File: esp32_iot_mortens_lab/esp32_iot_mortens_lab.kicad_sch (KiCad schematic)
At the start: 5 parts, among them P1 USB_C_Plug_USB2.0, Q1 UMH3N, U1 ESP32-WROOM-32D, U2 USBLC6-2P6, U3 CP2104

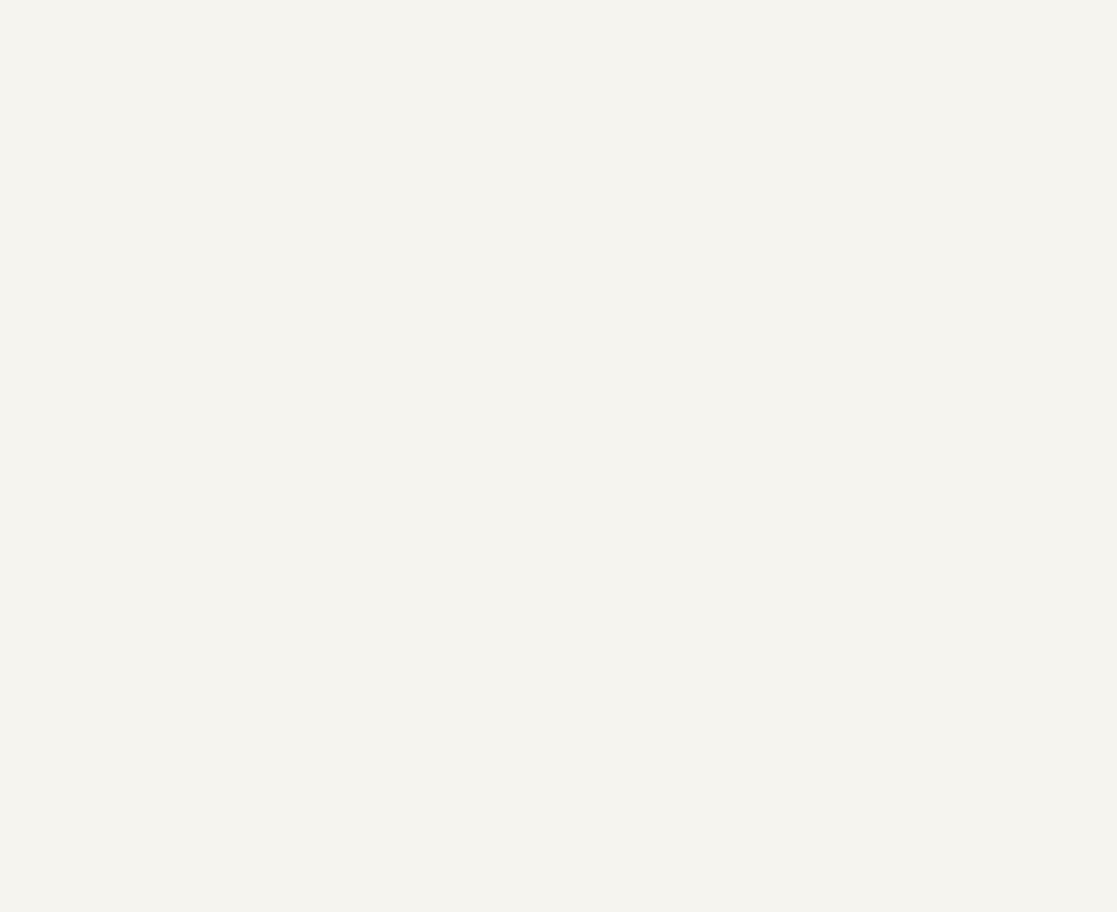
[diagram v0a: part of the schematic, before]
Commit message: upto J2 screw
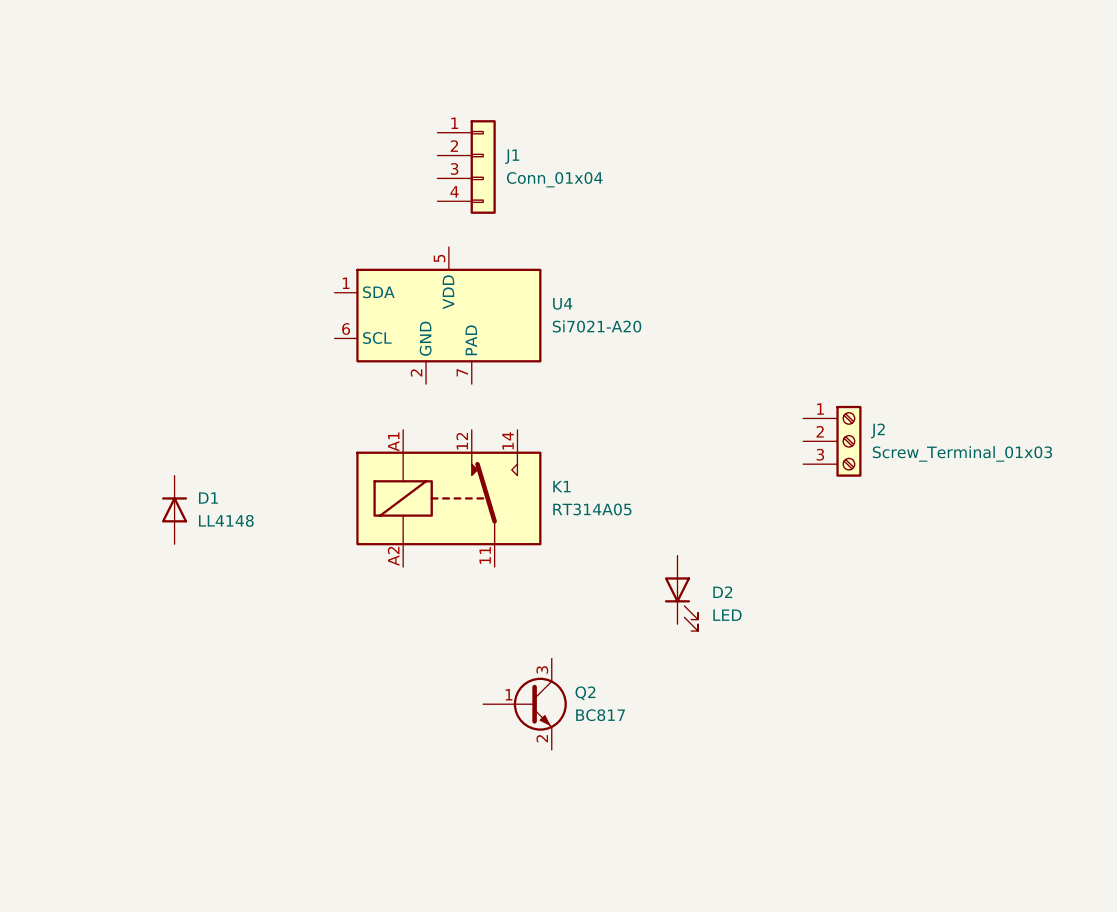
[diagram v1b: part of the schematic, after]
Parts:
- added D1: LL4148, Diode_SMD:D_MiniMELF, symbol Diode:LL4148
- added D2: LED, symbol Device:LED
- added J1: Conn_01x04, symbol Connector_Generic:Conn_01x04
- added J2: Screw_Terminal_01x03, symbol Connector:Screw_Terminal_01x03
- added K1: RT314A05, Relay_THT:Relay_SPDT_Schrack-RT1-16A-FormC_RM5mm, symbol Relay:RT314A05
- added Q2: BC817, Package_TO_SOT_SMD:SOT-23, symbol Transistor_BJT:BC817
- added U4: Si7021-A20, Package_DFN_QFN:DFN-6-1EP_3x3mm_P1mm_EP1.5x2.4mm, symbol Sensor_Humidity:Si7021-A20

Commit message: upto fuse & capacitance
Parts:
- added C1: C_Polarized_Small, symbol Device:C_Polarized_Small
- added F1: Fuse, symbol Device:Fuse
- added J3: Screw_Terminal_01x08, symbol Connector:Screw_Terminal_01x08
- added J4: Screw_Terminal_01x02, symbol Connector:Screw_Terminal_01x02
- added U5: 74HC245, symbol 74xx:74HC245

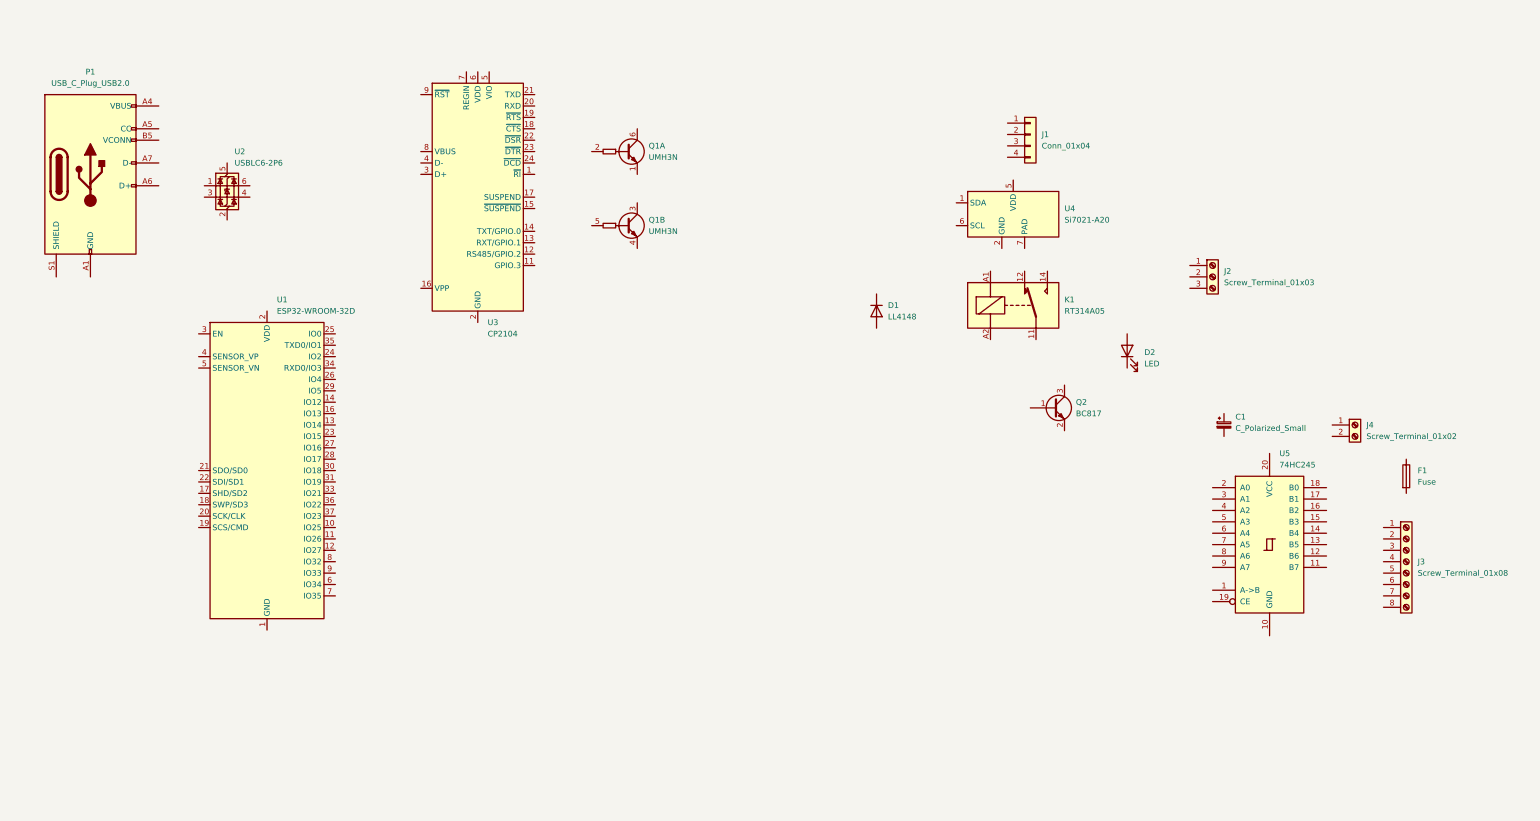
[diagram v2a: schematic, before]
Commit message: resistors to cc pins of usb_c
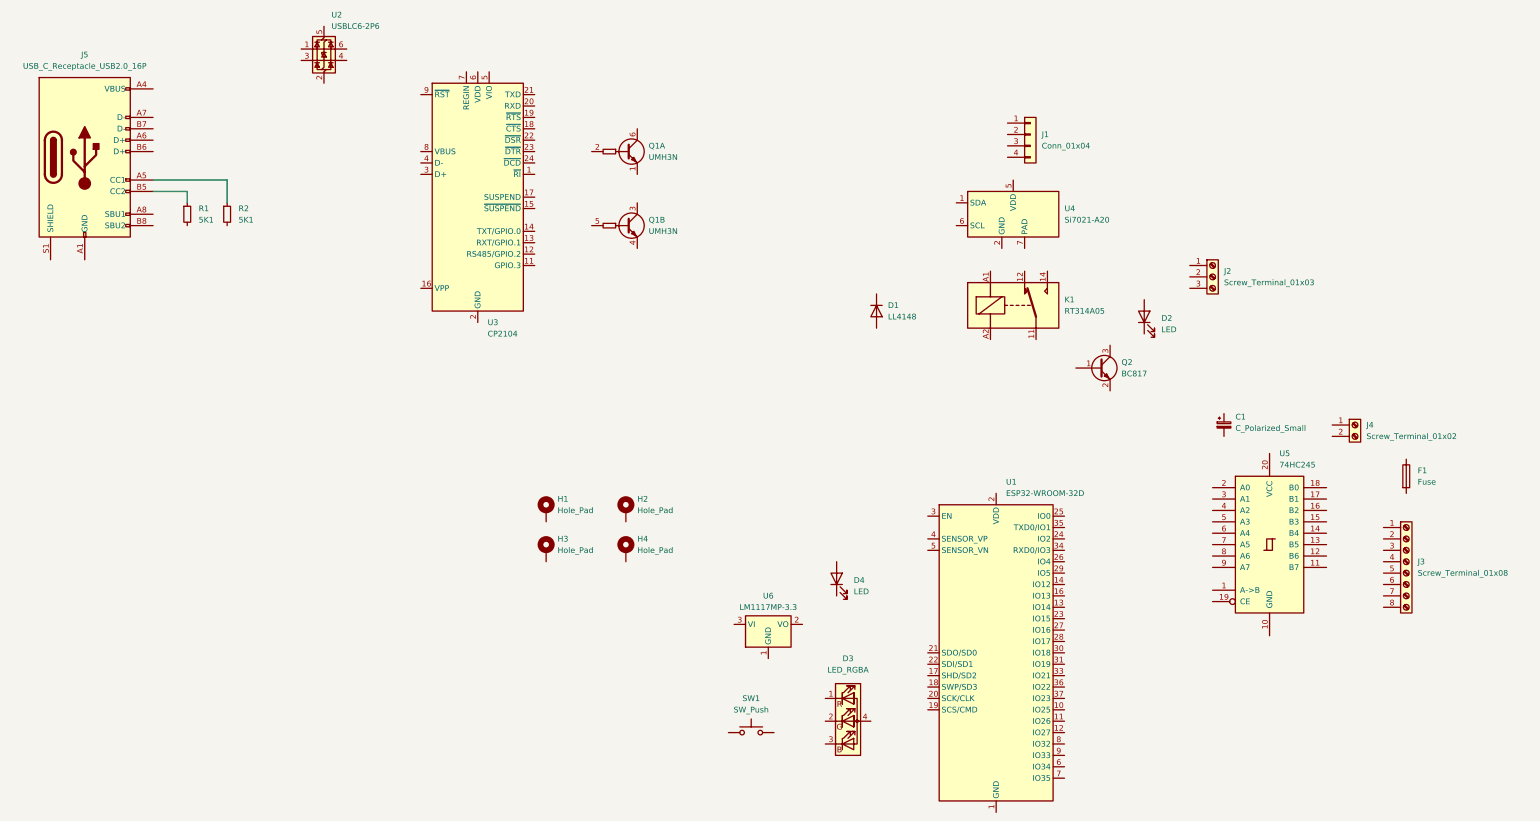
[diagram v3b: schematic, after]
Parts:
- removed P1: USB_C_Plug_USB2.0, symbol Connector:USB_C_Plug_USB2.0
- added D3: LED_RGBA, symbol Device:LED_RGBA
- added D4: LED, symbol Device:LED
- added H1, H2, H3, H4: Hole_Pad, symbol Mechanical:MountingHole_Pad
- added J5: USB_C_Receptacle_USB2.0_16P, symbol Connector:USB_C_Receptacle_USB2.0_16P
- added R1, R2: 5K1, symbol Device:R_Small
- added SW1: SW_Push, symbol Switch:SW_Push
- added U6: LM1117MP-3.3, Package_TO_SOT_SMD:SOT-223-3_TabPin2, symbol Regulator_Linear:LM1117MP-3.3
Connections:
- new net: J5.B5 (CC2), R1.1
- new net: J5.A5 (CC1), R2.1
- new net: J5.A1 (GND), J5.A12 (GND), J5.B1 (GND), J5.B12 (GND)
- new net: J5.A4 (VBUS), J5.A9 (VBUS), J5.B4 (VBUS), J5.B9 (VBUS)
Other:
- moved on the sheet: D2, Q2, U1, U2

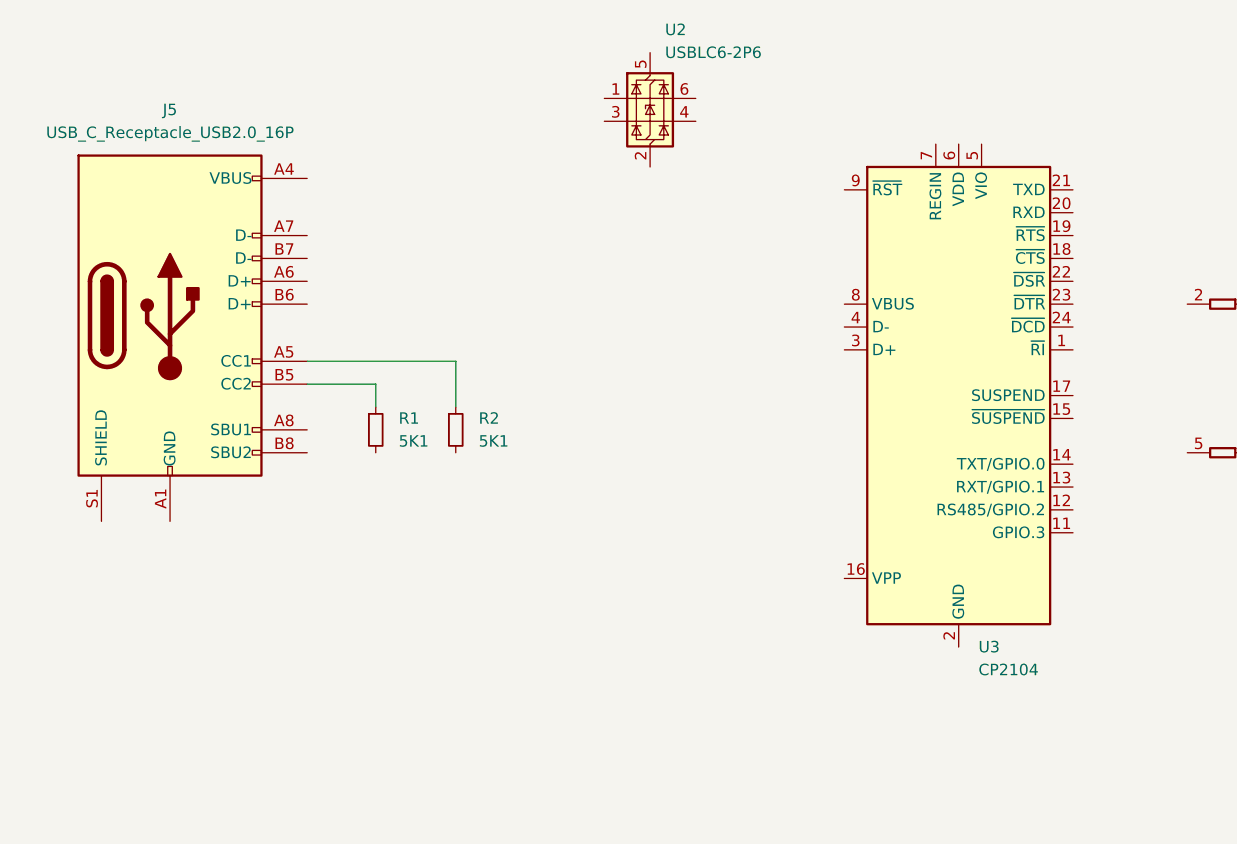
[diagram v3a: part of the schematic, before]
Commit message: usb-c to electrostatic discharge device
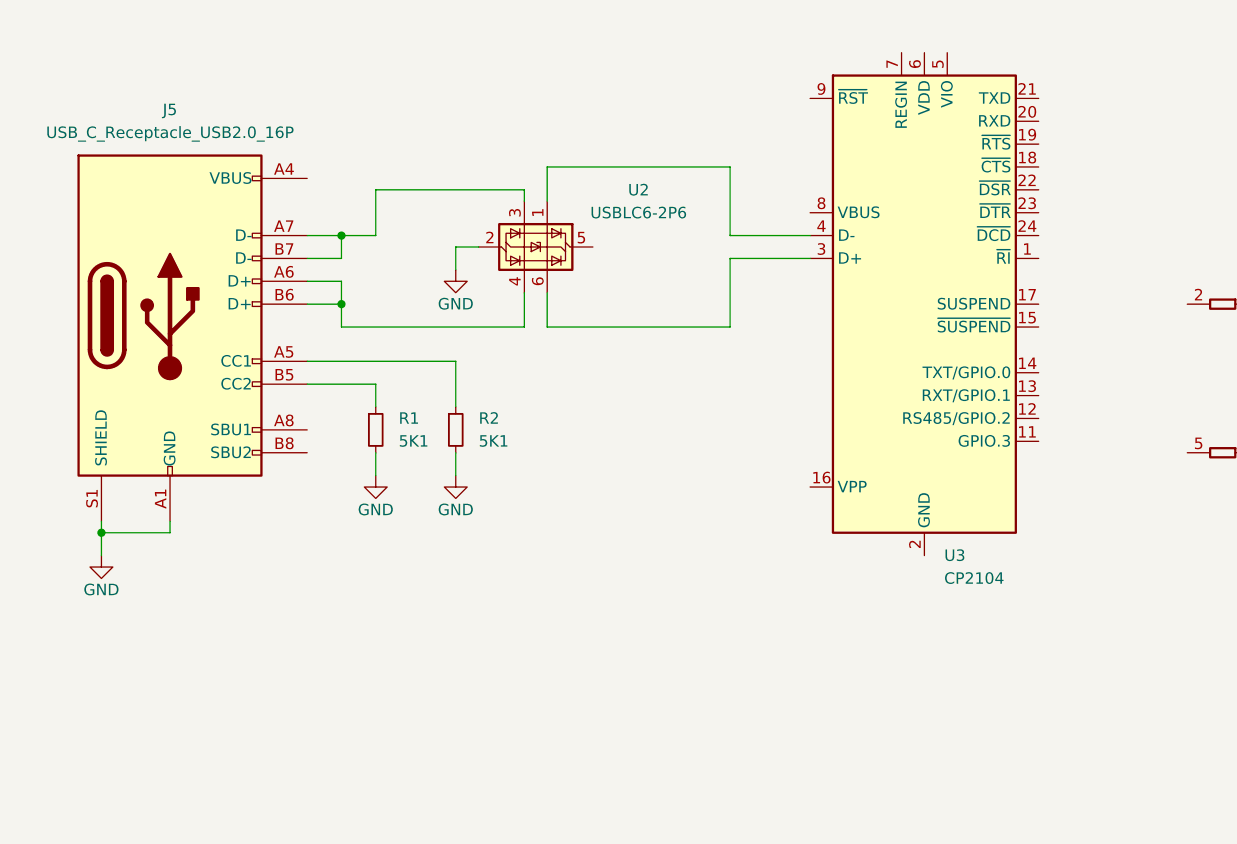
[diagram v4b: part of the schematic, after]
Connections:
- net at U2.1 (I/O1): now also U3.4 (D-)
- net GND: now reaches U2.2 (GND)
- net GND: now also J5.A1 (GND), J5.A12 (GND), J5.B1 (GND), J5.B12 (GND), J5.S1 (SHIELD), R1.2, R2.2
- net at U2.3 (I/O2): now also J5.A7 (D-), J5.B7 (D-)
- net at U2.4 (I/O2): now also J5.A6 (D+), J5.B6 (D+)
- net at U2.6 (I/O1): now also U3.3 (D+)
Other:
- moved on the sheet: U2, U3
